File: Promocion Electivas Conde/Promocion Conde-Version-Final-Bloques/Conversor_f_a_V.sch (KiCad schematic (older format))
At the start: 14 parts, among them J2 Bornera Señal de Entrada, Q1 BC848, U2 4040, U3 4070, U4 TL082

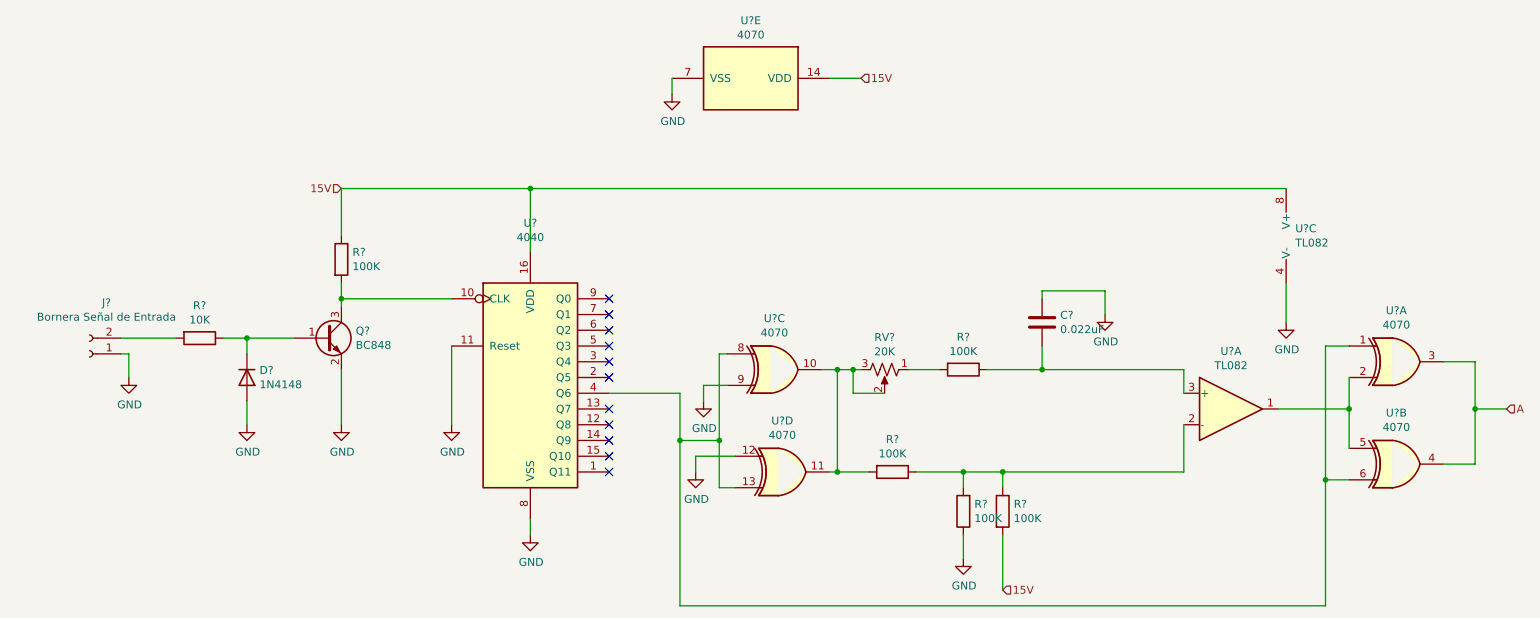
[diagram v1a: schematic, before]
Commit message: Bloques y footprint asignados
Falta elegir y asignar el de los potenciometros Rv3 y Rv7.
Las salidas K3 y K20 también...
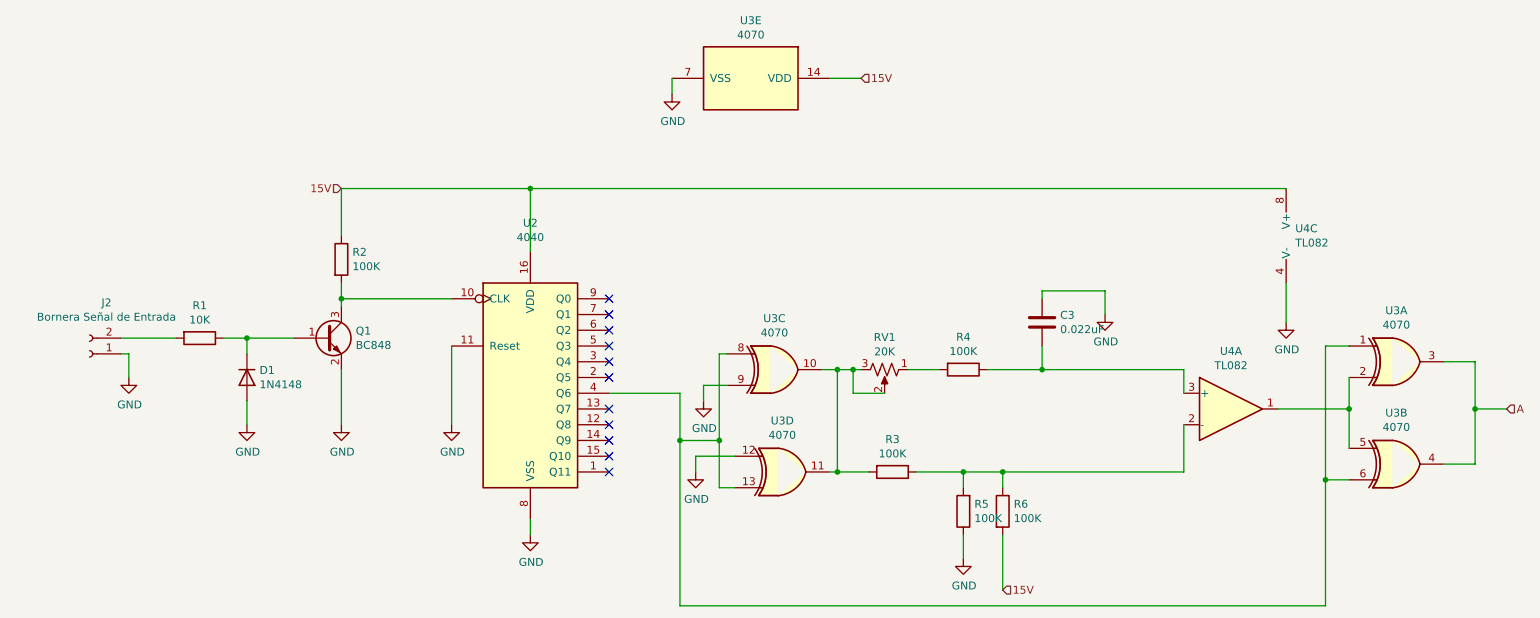
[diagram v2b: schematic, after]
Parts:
- RV1: footprint (none) -> Resistor_SMD:R_0603_1608Metric_Pad0.98x0.95mm_HandSolder
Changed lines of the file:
@@
 $Descr A4 11693 8268
 encoding utf-8
-Sheet 5 5
+Sheet 2 6
 Title ""
 Date ""
@@
 AR Path="/612E15A4/61312797" Ref="R2"  Part="1"
 AR Path="/6184FF73/61312797" Ref="R?"  Part="1"
-F 0 "R?" H 2920 2146 50  0000 L CNN
+F 0 "R2" H 2920 2146 50  0000 L CNN
 F 1 "100K" H 2920 2055 50  0000 L CNN
 F 2 "Resistor_SMD:R_0603_1608Metric_Pad0.98x0.95mm_HandSolder" V 2780 2100 50  0001 C CNN
@@
 AR Path="/612E15A4/6131279D" Ref="Q1"  Part="1"
 AR Path="/6184FF73/6131279D" Ref="Q?"  Part="1"
-F 0 "Q?" H 2941 2646 50  0000 L CNN
+F 0 "Q1" H 2941 2646 50  0000 L CNN
 F 1 "BC848" H 2941 2555 50  0000 L CNN
 F 2 "Package_TO_SOT_SMD:SOT-23" H 2950 2525 50  0001 L CIN
@@
 AR Path="/612E15A4/613127A3" Ref="D1"  Part="1"
 AR Path="/6184FF73/613127A3" Ref="D?"  Part="1"
-F 0 "D?" V 2204 2930 50  0000 L CNN
+F 0 "D1" V 2204 2930 50  0000 L CNN
 F 1 "1N4148" V 2295 2930 50  0000 L CNN
 F 2 "Diode_THT:D_DO-35_SOD27_P7.62mm_Horizontal" H 2250 2675 50  0001 C CNN
@@
 AR Path="/612E15A4/613127A9" Ref="R1"  Part="1"
 AR Path="/6184FF73/613127A9" Ref="R?"  Part="1"
-F 0 "R?" V 1743 2600 50  0000 C CNN
+F 0 "R1" V 1743 2600 50  0000 C CNN
 F 1 "10K" V 1834 2600 50  0000 C CNN
 F 2 "Resistor_SMD:R_0603_1608Metric_Pad0.98x0.95mm_HandSolder" V 1880 2600 50  0001 C CNN
@@
 AR Path="/612E15A4/613127AF" Ref="#PWR0101"  Part="1"
 AR Path="/6184FF73/613127AF" Ref="#PWR?"  Part="1"
-F 0 "#PWR?" H 2250 2900 50  0001 C CNN
+F 0 "#PWR0101" H 2250 2900 50  0001 C CNN
 F 1 "GND" H 2255 2977 50  0000 C CNN
 F 2 "" H 2250 3150 50  0001 C CNN
@@
 AR Path="/612E15A4/613127B5" Ref="#PWR0102"  Part="1"
 AR Path="/6184FF73/613127B5" Ref="#PWR?"  Part="1"
-F 0 "#PWR?" H 2850 2900 50  0001 C CNN
+F 0 "#PWR0102" H 2850 2900 50  0001 C CNN
 F 1 "GND" H 2855 2977 50  0000 C CNN
 F 2 "" H 2850 3150 50  0001 C CNN
@@
 AR Path="/612E15A4/613127BB" Ref="U2"  Part="1"
 AR Path="/6184FF73/613127BB" Ref="U?"  Part="1"
-F 0 "U?" H 4050 3831 50  0000 C CNN
+F 0 "U2" H 4050 3831 50  0000 C CNN
 F 1 "4040" H 4050 3740 50  0000 C CNN
 F 2 "Package_SO:SOIC-16_3.9x9.9mm_P1.27mm" H 4050 2850 50  0001 C CNN
@@
 AR Path="/612E15A4/613127C1" Ref="#PWR0103"  Part="1"
 AR Path="/6184FF73/613127C1" Ref="#PWR?"  Part="1"
-F 0 "#PWR?" H 3550 2900 50  0001 C CNN
+F 0 "#PWR0103" H 3550 2900 50  0001 C CNN
 F 1 "GND" H 3555 2977 50  0000 C CNN
 F 2 "" H 3550 3150 50  0001 C CNN
@@
 AR Path="/612E15A4/613127C7" Ref="#PWR0104"  Part="1"
 AR Path="/6184FF73/613127C7" Ref="#PWR?"  Part="1"
-F 0 "#PWR?" H 4050 3600 50  0001 C CNN
+F 0 "#PWR0104" H 4050 3600 50  0001 C CNN
 F 1 "GND" H 4055 3677 50  0000 C CNN
 F 2 "" H 4050 3850 50  0001 C CNN
@@
 AR Path="/612E15A4/613127CD" Ref="U3"  Part="1"
 AR Path="/6184FF73/613127CD" Ref="U?"  Part="1"
-F 0 "U?" H 9550 3075 50  0000 C CNN
+F 0 "U3" H 9550 3075 50  0000 C CNN
 F 1 "4070" H 9550 2984 50  0000 C CNN
 F 2 "" H 9550 2750 50  0001 C CNN
@@
 AR Path="/612E15A4/613127D3" Ref="U3"  Part="2"
 AR Path="/6184FF73/613127D3" Ref="U?"  Part="2"
-F 0 "U?" H 9550 3725 50  0000 C CNN
+F 0 "U3" H 9550 3725 50  0000 C CNN
 F 1 "4070" H 9550 3634 50  0000 C CNN
 F 2 "" H 9550 3400 50  0001 C CNN
@@
 AR Path="/612E15A4/613127D9" Ref="U3"  Part="3"
 AR Path="/6184FF73/613127D9" Ref="U?"  Part="3"
-F 0 "U?" H 5600 3125 50  0000 C CNN
+F 0 "U3" H 5600 3125 50  0000 C CNN
 F 1 "4070" H 5600 3034 50  0000 C CNN
 F 2 "" H 5600 2800 50  0001 C CNN
@@
 AR Path="/612E15A4/613127DF" Ref="U3"  Part="5"
 AR Path="/6184FF73/613127DF" Ref="U?"  Part="5"
-F 0 "U?" V 5083 950 50  0000 C CNN
+F 0 "U3" V 5083 950 50  0000 C CNN
 F 1 "4070" V 5174 950 50  0000 C CNN
 F 2 "" H 5450 950 50  0001 C CNN
@@
 AR Path="/612E15A4/613127E5" Ref="R3"  Part="1"
 AR Path="/6184FF73/613127E5" Ref="R?"  Part="1"
-F 0 "R?" V 6143 3450 50  0000 C CNN
+F 0 "R3" V 6143 3450 50  0000 C CNN
 F 1 "100K" V 6234 3450 50  0000 C CNN
 F 2 "Resistor_SMD:R_0603_1608Metric_Pad0.98x0.95mm_HandSolder" V 6280 3450 50  0001 C CNN
@@
 AR Path="/612E15A4/613127EB" Ref="R5"  Part="1"
 AR Path="/6184FF73/613127EB" Ref="R?"  Part="1"
-F 0 "R?" H 6730 3654 50  0000 R CNN
+F 0 "R5" H 6730 3654 50  0000 R CNN
 F 1 "100K" H 6730 3745 50  0000 R CNN
 F 2 "Resistor_SMD:R_0603_1608Metric_Pad0.98x0.95mm_HandSolder" V 6730 3700 50  0001 C CNN
@@
 AR Path="/612E15A4/613127F1" Ref="R6"  Part="1"
 AR Path="/6184FF73/613127F1" Ref="R?"  Part="1"
-F 0 "R?" H 7120 3746 50  0000 L CNN
+F 0 "R6" H 7120 3746 50  0000 L CNN
 F 1 "100K" H 7120 3655 50  0000 L CNN
 F 2 "Resistor_SMD:R_0603_1608Metric_Pad0.98x0.95mm_HandSolder" V 6980 3700 50  0001 C CNN
@@
 AR Path="/612E15A4/613127F7" Ref="R4"  Part="1"
 AR Path="/6184FF73/613127F7" Ref="R?"  Part="1"
-F 0 "R?" V 6593 2800 50  0000 C CNN
+F 0 "R4" V 6593 2800 50  0000 C CNN
 F 1 "100K" V 6684 2800 50  0000 C CNN
 F 2 "Resistor_SMD:R_0603_1608Metric_Pad0.98x0.95mm_HandSolder" V 6730 2800 50  0001 C CNN
@@
 AR Path="/612E15A4/613127FD" Ref="U4"  Part="1"
 AR Path="/6184FF73/613127FD" Ref="U?"  Part="1"
-F 0 "U?" H 8500 3417 50  0000 C CNN
+F 0 "U4" H 8500 3417 50  0000 C CNN
 F 1 "TL082" H 8500 3326 50  0000 C CNN
 F 2 "Package_SO:SOIC-8-1EP_3.9x4.9mm_P1.27mm_EP2.29x3mm" H 8500 3050 50  0001 C CNN
@@
 AR Path="/612E15A4/61312803" Ref="J2"  Part="1"
 AR Path="/6184FF73/61312803" Ref="J?"  Part="1"
-F 0 "J?" H 1142 2375 50  0000 C CNN
+F 0 "J2" H 1142 2375 50  0000 C CNN
 F 1 "Bornera Señal de Entrada" H 1142 2466 50  0000 C CNN
 F 2 "" H 1250 2700 50  0001 C CNN
@@
 AR Path="/612E15A4/61312815" Ref="#PWR0105"  Part="1"
 AR Path="/6184FF73/61312815" Ref="#PWR?"  Part="1"
-F 0 "#PWR?" H 5100 3200 50  0001 C CNN
+F 0 "#PWR0105" H 5100 3200 50  0001 C CNN
 F 1 "GND" H 5105 3277 50  0000 C CNN
 F 2 "" H 5100 3450 50  0001 C CNN
@@
 AR Path="/612E15A4/6131281B" Ref="#PWR0106"  Part="1"
 AR Path="/6184FF73/6131281B" Ref="#PWR?"  Part="1"
-F 0 "#PWR?" H 5150 2750 50  0001 C CNN
+F 0 "#PWR0106" H 5150 2750 50  0001 C CNN
 F 1 "GND" H 5155 2827 50  0000 C CNN
 F 2 "" H 5150 3000 50  0001 C CNN
@@
 AR Path="/612E15A4/61312824" Ref="RV1"  Part="1"
 AR Path="/6184FF73/61312824" Ref="RV?"  Part="1"
-F 0 "RV?" V 6095 2800 50  0000 C CNN
+F 0 "RV1" V 6095 2800 50  0000 C CNN
 F 1 "20K" V 6186 2800 50  0000 C CNN
-F 2 "" H 6300 2800 50  0001 C CNN
+F 2 "Resistor_SMD:R_0603_1608Metric_Pad0.98x0.95mm_HandSolder" H 6300 2800 50  0001 C CNN
 F 3 "~" H 6300 2800 50  0001 C CNN
 	1    6300 2800
@@
 AR Path="/612E15A4/6131282E" Ref="C3"  Part="1"
 AR Path="/6184FF73/6131282E" Ref="C?"  Part="1"
-F 0 "C?" H 7415 2546 50  0000 L CNN
+F 0 "C3" H 7415 2546 50  0000 L CNN
 F 1 "0.022uF" H 7415 2455 50  0000 L CNN
 F 2 "Capacitor_SMD:C_0603_1608Metric_Pad1.08x0.95mm_HandSolder" H 7338 2350 50  0001 C CNN
@@
 AR Path="/612E15A4/61312836" Ref="U3"  Part="4"
 AR Path="/6184FF73/61312836" Ref="U?"  Part="4"
-F 0 "U?" H 5650 3775 50  0000 C CNN
+F 0 "U3" H 5650 3775 50  0000 C CNN
 F 1 "4070" H 5650 3684 50  0000 C CNN
 F 2 "" H 5650 3450 50  0001 C CNN
@@
 AR Path="/612E15A4/61312847" Ref="#PWR0107"  Part="1"
 AR Path="/6184FF73/61312847" Ref="#PWR?"  Part="1"
-F 0 "#PWR?" H 6800 3750 50  0001 C CNN
+F 0 "#PWR0107" H 6800 3750 50  0001 C CNN
 F 1 "GND" H 6805 3827 50  0000 C CNN
 F 2 "" H 6800 4000 50  0001 C CNN
@@
 AR Path="/612E15A4/61312853" Ref="#PWR0108"  Part="1"
 AR Path="/6184FF73/61312853" Ref="#PWR?"  Part="1"
-F 0 "#PWR?" H 7700 2200 50  0001 C CNN
+F 0 "#PWR0108" H 7700 2200 50  0001 C CNN
 F 1 "GND" H 7705 2277 50  0000 C CNN
 F 2 "" H 7700 2450 50  0001 C CNN
@@
 AR Path="/612E15A4/6131285F" Ref="U4"  Part="3"
 AR Path="/6184FF73/6131285F" Ref="U?"  Part="3"
-F 0 "U?" H 8908 1996 50  0000 L CNN
+F 0 "U4" H 8908 1996 50  0000 L CNN
 F 1 "TL082" H 8908 1905 50  0000 L CNN
 F 2 "Package_SO:SOIC-8-1EP_3.9x4.9mm_P1.27mm_EP2.29x3mm" H 8950 1950 50  0001 C CNN
@@
 AR Path="/612E15A4/61312865" Ref="#PWR0109"  Part="1"
 AR Path="/6184FF73/61312865" Ref="#PWR?"  Part="1"
-F 0 "#PWR?" H 8850 2250 50  0001 C CNN
+F 0 "#PWR0109" H 8850 2250 50  0001 C CNN
 F 1 "GND" H 8855 2327 50  0000 C CNN
 F 2 "" H 8850 2500 50  0001 C CNN
@@
 AR Path="/612E15A4/6131287A" Ref="#PWR0110"  Part="1"
 AR Path="/6184FF73/6131287A" Ref="#PWR?"  Part="1"
-F 0 "#PWR?" H 4950 800 50  0001 C CNN
+F 0 "#PWR0110" H 4950 800 50  0001 C CNN
 F 1 "GND" H 4955 877 50  0000 C CNN
 F 2 "" H 4950 1050 50  0001 C CNN
@@
 AR Path="/612E15A4/613128BC" Ref="#PWR0111"  Part="1"
 AR Path="/6184FF73/613128BC" Ref="#PWR?"  Part="1"
-F 0 "#PWR?" H 1500 2600 50  0001 C CNN
+F 0 "#PWR0111" H 1500 2600 50  0001 C CNN
 F 1 "GND" H 1505 2677 50  0000 C CNN
 F 2 "" H 1500 2850 50  0001 C CNN

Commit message: Actualizacion esquemático en bloques
Asignacion de la huella de la compuerta or (soic-14) y se creó la huella del convertidor DC-DC que se va a usar en la alimentacion (falta generar la forma en el esquemático)
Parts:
- U3: footprint (none) -> Package_SO:SOIC-14_3.9x8.7mm_P1.27mm
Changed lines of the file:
@@
 F 0 "U3" H 9550 3075 50  0000 C CNN
 F 1 "4070" H 9550 2984 50  0000 C CNN
-F 2 "" H 9550 2750 50  0001 C CNN
+F 2 "Package_SO:SOIC-14_3.9x8.7mm_P1.27mm" H 9550 2750 50  0001 C CNN
 F 3 "https://www.digikey.com/es/products/detail/texas-instruments/CD4070BMT/1691302" H 9550 2750 50  0001 C CNN
 	1    9550 2750
@@
 F 0 "U3" H 9550 3725 50  0000 C CNN
 F 1 "4070" H 9550 3634 50  0000 C CNN
-F 2 "" H 9550 3400 50  0001 C CNN
+F 2 "Package_SO:SOIC-14_3.9x8.7mm_P1.27mm" H 9550 3400 50  0001 C CNN
 F 3 "https://www.digikey.com/es/products/detail/texas-instruments/CD4070BMT/1691302" H 9550 3400 50  0001 C CNN
 	2    9550 3400
@@
 F 0 "U3" H 5600 3125 50  0000 C CNN
 F 1 "4070" H 5600 3034 50  0000 C CNN
-F 2 "" H 5600 2800 50  0001 C CNN
+F 2 "Package_SO:SOIC-14_3.9x8.7mm_P1.27mm" H 5600 2800 50  0001 C CNN
 F 3 "https://www.digikey.com/es/products/detail/texas-instruments/CD4070BMT/1691302" H 5600 2800 50  0001 C CNN
 	3    5600 2800
@@
 F 0 "U3" V 5083 950 50  0000 C CNN
 F 1 "4070" V 5174 950 50  0000 C CNN
-F 2 "" H 5450 950 50  0001 C CNN
+F 2 "Package_SO:SOIC-14_3.9x8.7mm_P1.27mm" H 5450 950 50  0001 C CNN
 F 3 "https://www.digikey.com/es/products/detail/texas-instruments/CD4070BMT/1691302" H 5450 950 50  0001 C CNN
 	5    5450 950
@@
 F 0 "U3" H 5650 3775 50  0000 C CNN
 F 1 "4070" H 5650 3684 50  0000 C CNN
-F 2 "" H 5650 3450 50  0001 C CNN
+F 2 "Package_SO:SOIC-14_3.9x8.7mm_P1.27mm" H 5650 3450 50  0001 C CNN
 F 3 "https://www.digikey.com/es/products/detail/texas-instruments/CD4070BMT/1691302" H 5650 3450 50  0001 C CNN
 	4    5650 3450

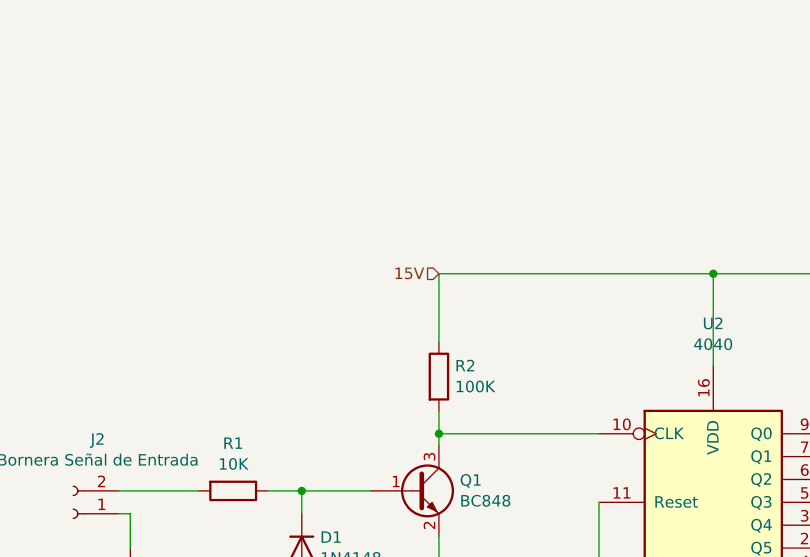
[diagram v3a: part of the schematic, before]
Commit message: Actualizacion Convertidor
Se creó el esquemático del convertidor y se hizo la conexión del mismo
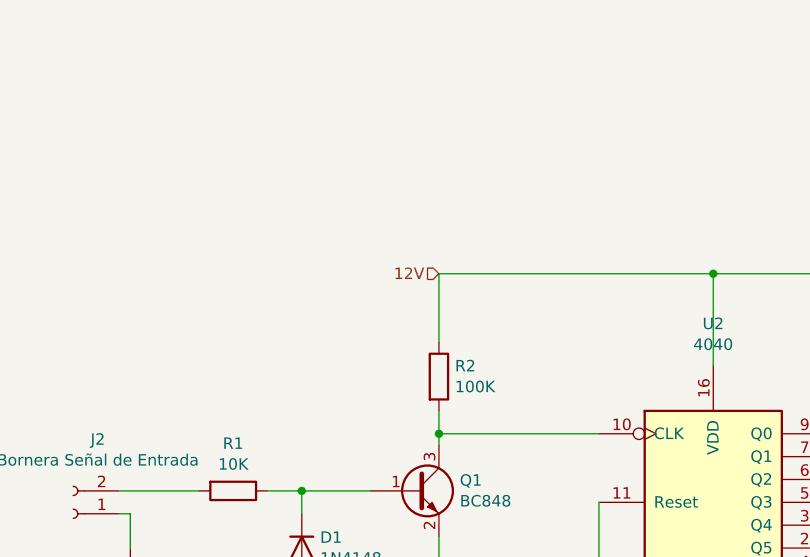
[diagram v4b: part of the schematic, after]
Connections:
- net 15V: no longer R2.1, U2.16 (VDD), U4.8 (V+)
- new net 12V: R2.1, U2.16 (VDD), U4.8 (V+)
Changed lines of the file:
@@
 Connection ~ 4050 1650
 Text HLabel 2850 1650 0    50   Input ~ 0
-15V
+12V
 Text HLabel 7050 4200 2    50   Input ~ 0
 15V

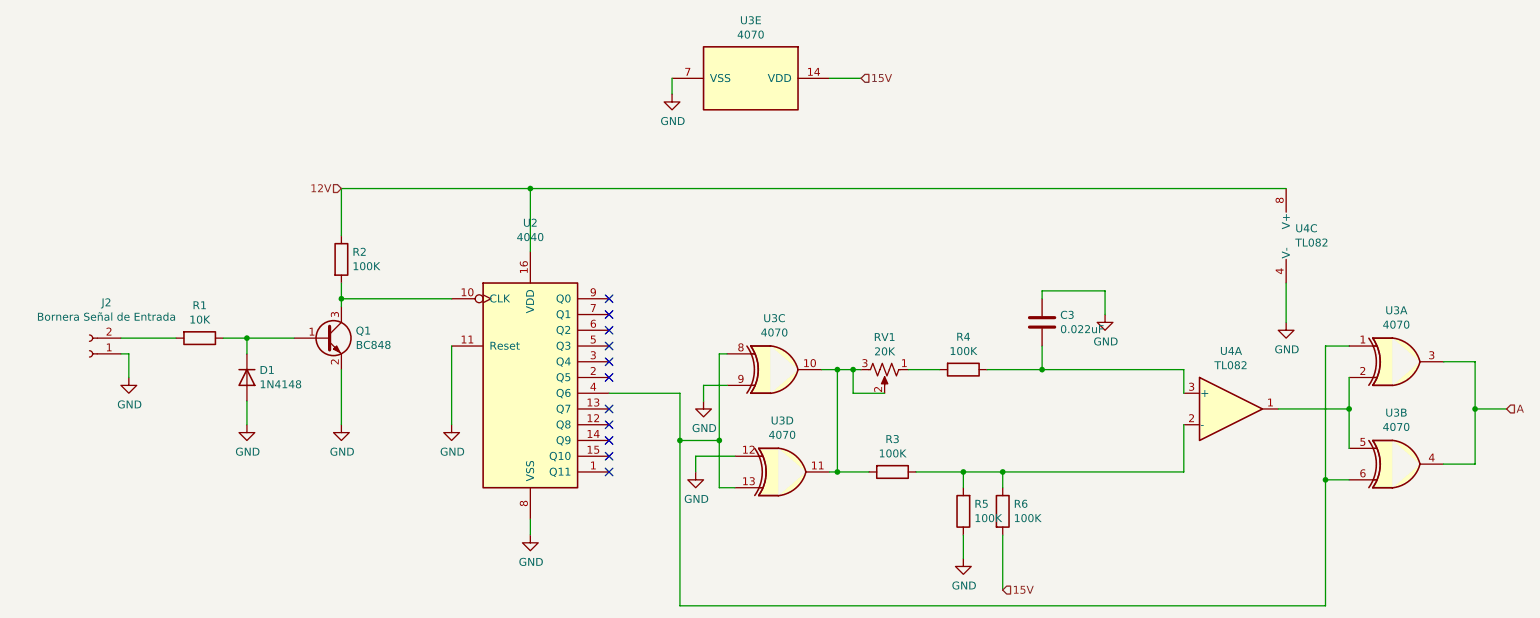
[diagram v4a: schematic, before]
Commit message: Actualizacion
Actualizo los footprints del esquematico y se inicia el PCB
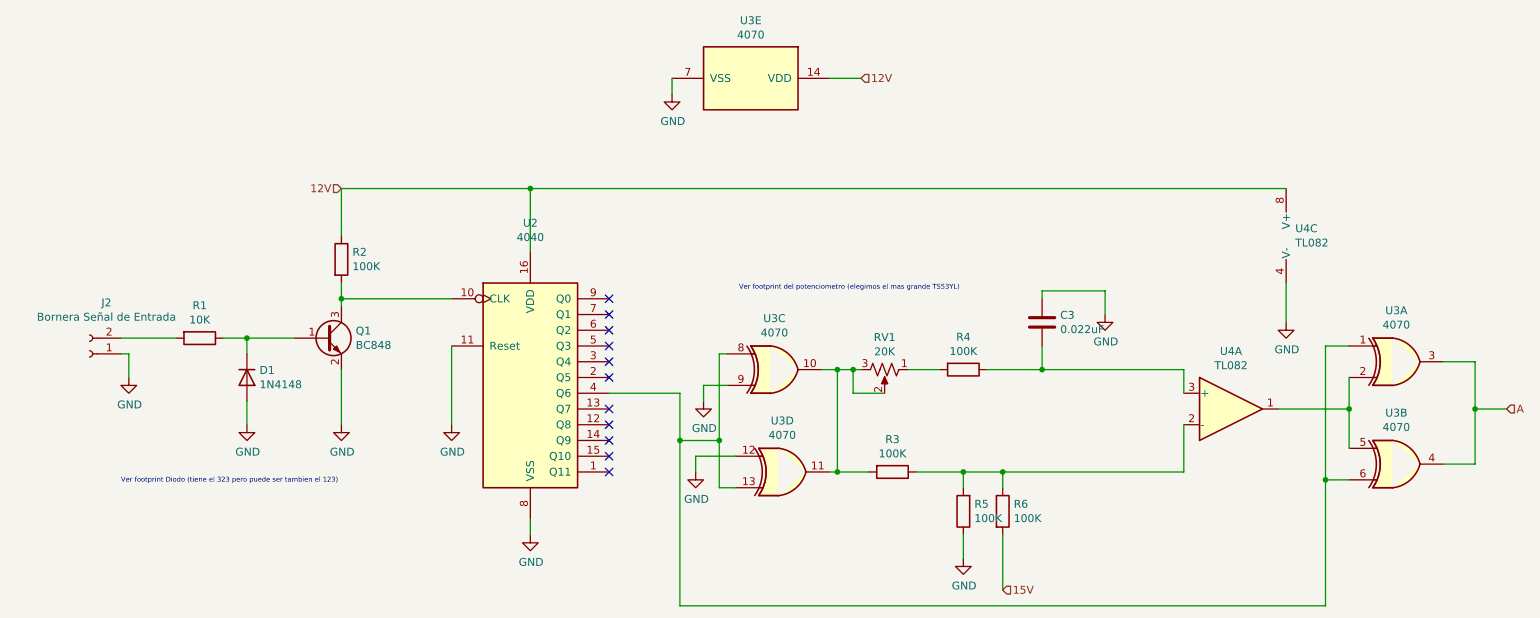
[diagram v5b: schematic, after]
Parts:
- D1: footprint Diode_THT:D_DO-35_SOD27_P7.62mm_Horizontal -> Diode_SMD:D_SOD-323
- RV1: footprint Resistor_SMD:R_0603_1608Metric_Pad0.98x0.95mm_HandSolder -> Potentiometer_SMD:Potentiometer_Vishay_TS53YL_Vertical
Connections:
- net 12V: now also U3.14 (VDD)
- net 15V: no longer U3.14 (VDD)
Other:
- note added: "Ver footprint Diodo (tiene el 323 pero puede ser tambien el 123)"
- note added: "Ver footprint del potenciometro (elegimos el mas grande TS53YL)"
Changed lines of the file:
@@
 F 0 "D1" V 2204 2930 50  0000 L CNN
 F 1 "1N4148" V 2295 2930 50  0000 L CNN
-F 2 "Diode_THT:D_DO-35_SOD27_P7.62mm_Horizontal" H 2250 2675 50  0001 C CNN
-F 3 "https://assets.nexperia.com/documents/data-sheet/1N4148_1N4448.pdf" H 2250 2850 50  0001 C CNN
+F 2 "Diode_SMD:D_SOD-323" H 2250 2675 50  0001 C CNN
+F 3 "https://www.diodes.com/assets/Datasheets/1N4148WSF.pdf" H 2250 2850 50  0001 C CNN
 	1    2250 2850
 	0    1    1    0
@@
 F 0 "RV1" V 6095 2800 50  0000 C CNN
 F 1 "20K" V 6186 2800 50  0000 C CNN
-F 2 "Resistor_SMD:R_0603_1608Metric_Pad0.98x0.95mm_HandSolder" H 6300 2800 50  0001 C CNN
-F 3 "~" H 6300 2800 50  0001 C CNN
+F 2 "Potentiometer_SMD:Potentiometer_Vishay_TS53YL_Vertical" H 6300 2800 50  0001 C CNN
+F 3 "https://www.vishay.com/docs/51008/ts53.pdf" H 6300 2800 50  0001 C CNN
 	1    6300 2800
 	0    1    1    0
@@
 15V
 Text HLabel 6150 950  2    50   Input ~ 0
-15V
+12V
 Wire Wire Line
 	6150 950  5950 950
 Wire Wire Line
 	4050 1650 8850 1650
+Text Notes 5375 2300 0    31   ~ 0
+Ver footprint del potenciometro (elegimos el mas grande TS53YL)
+Text Notes 1450 3525 0    31   ~ 0
+Ver footprint Diodo (tiene el 323 pero puede ser tambien el 123)
 $EndSCHEMATC
